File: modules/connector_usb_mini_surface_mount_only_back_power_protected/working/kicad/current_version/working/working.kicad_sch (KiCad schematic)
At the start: 2 parts, among them J1 scumnsmo

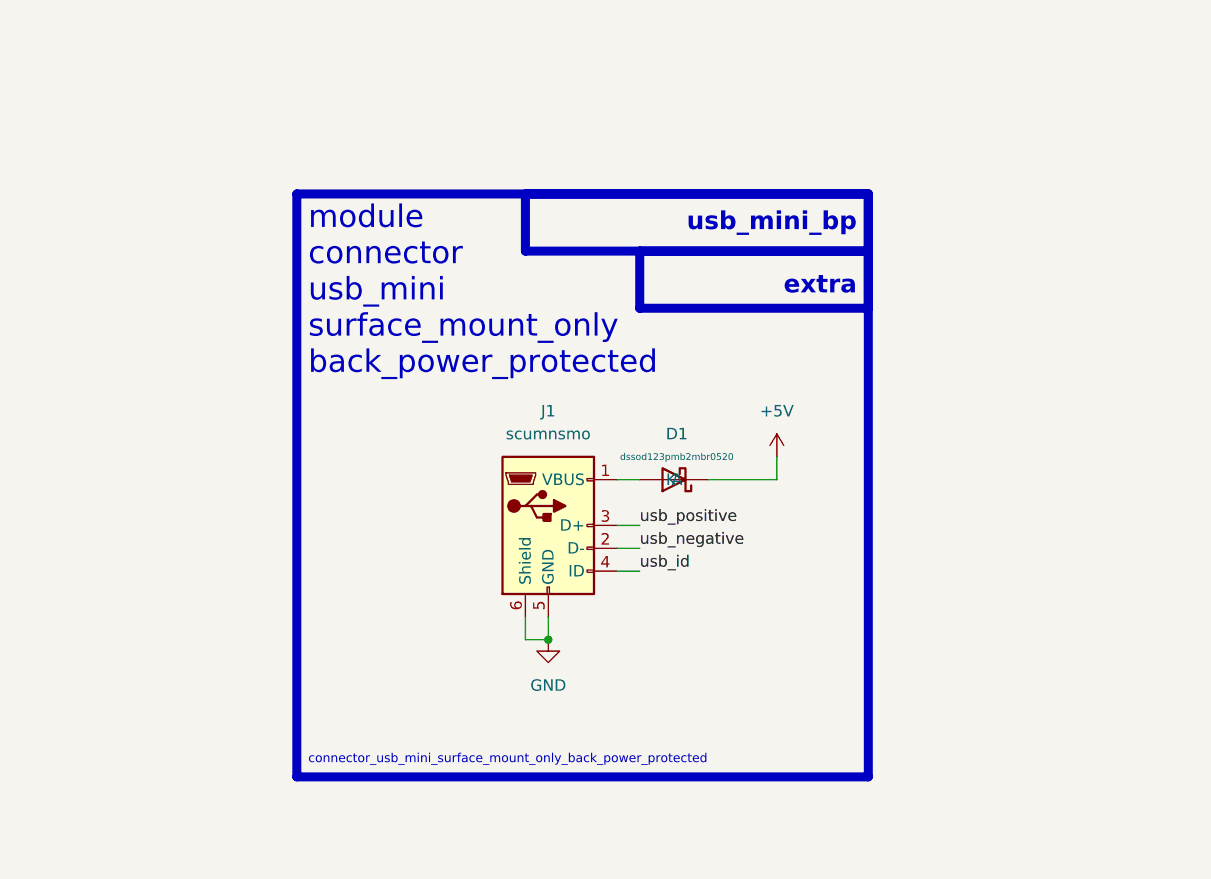
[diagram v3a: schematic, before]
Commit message: schematic formatting
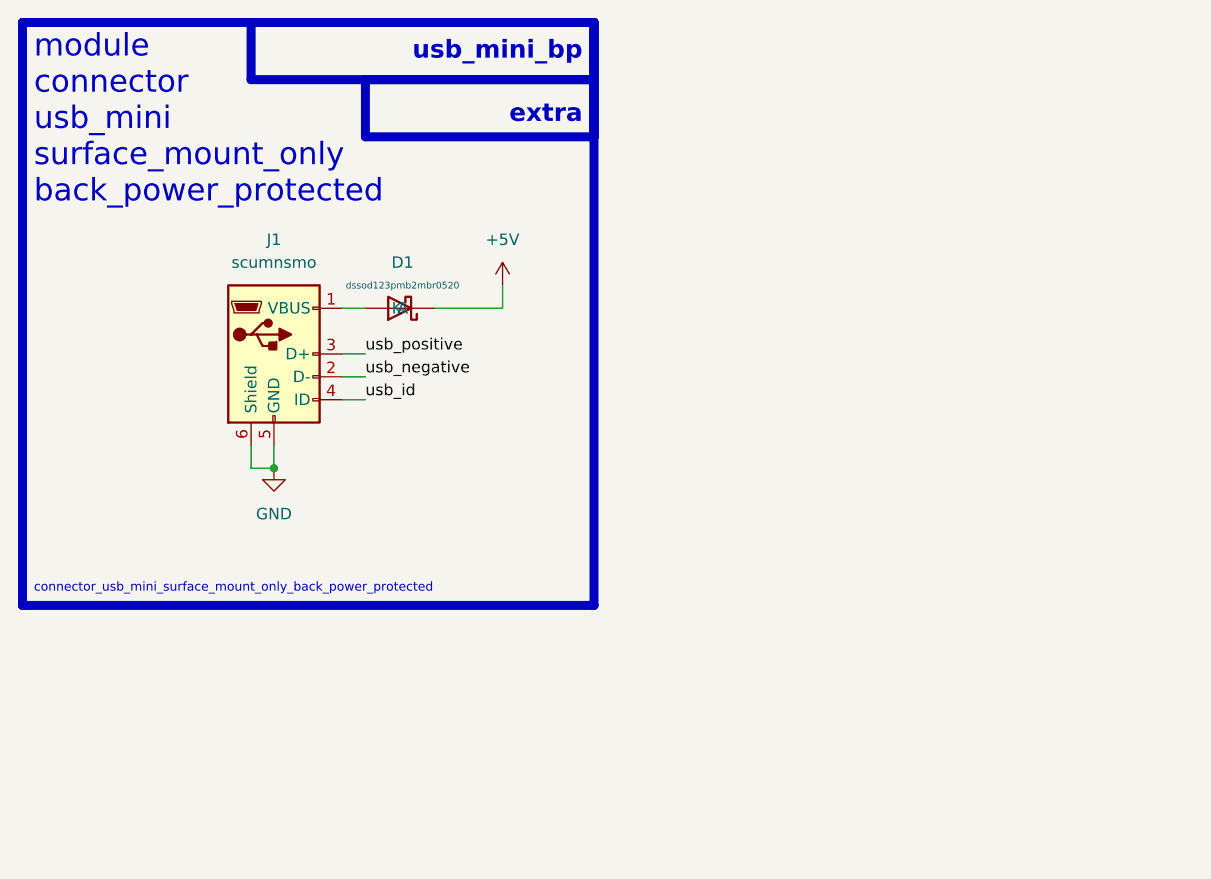
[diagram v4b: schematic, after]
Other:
- moved on the sheet: D1, J1
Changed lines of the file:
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@@
 (kicad_sch (version 20230121) (generator eeschema)
-  (paper "A4")
-  (junction (at 129.54 105.41) (diameter 0) (color 0 0 0 0)
+  (paper "A5")
+  (junction (at 99.06 86.36) (diameter 0) (color 0 0 0 0)
   )
-  (wire (pts (xy 129.54 102.87) (xy 129.54 105.41))
+  (wire (pts (xy 99.06 83.82) (xy 99.06 86.36))
     (stroke (width 0) (type default))
   )
-  (wire (pts (xy 137.16 87.63) (xy 139.7 87.63))
+  (wire (pts (xy 106.68 68.58) (xy 109.22 68.58))
     (stroke (width 0) (type default))
   )
-  (wire (pts (xy 137.16 97.79) (xy 139.7 97.79))
+  (wire (pts (xy 106.68 78.74) (xy 109.22 78.74))
     (stroke (width 0) (type default))
   )
-  (wire (pts (xy 137.16 95.25) (xy 139.7 95.25))
+  (wire (pts (xy 106.68 76.2) (xy 109.22 76.2))
     (stroke (width 0) (type default))
   )
-  (wire (pts (xy 154.94 85.09) (xy 154.94 87.63))
+  (wire (pts (xy 124.46 66.04) (xy 124.46 68.58))
     (stroke (width 0) (type default))
   )
-  (wire (pts (xy 154.94 87.63) (xy 147.32 87.63))
+  (wire (pts (xy 124.46 68.58) (xy 116.84 68.58))
     (stroke (width 0) (type default))
   )
-  (wire (pts (xy 127 105.41) (xy 129.54 105.41))
+  (wire (pts (xy 96.52 86.36) (xy 99.06 86.36))
     (stroke (width 0) (type default))
   )
-  (wire (pts (xy 127 102.87) (xy 127 105.41))
+  (wire (pts (xy 96.52 83.82) (xy 96.52 86.36))
     (stroke (width 0) (type default))
   )
-  (wire (pts (xy 137.16 92.71) (xy 139.7 92.71))
+  (wire (pts (xy 106.68 73.66) (xy 109.22 73.66))
     (stroke (width 0) (type default))
   )
-  (rectangle (start 127 55.88) (end 165.1 62.23)
+  (rectangle (start 96.52 36.83) (end 134.62 43.18)
     (stroke (width 1) (type default))
     (fill (type none))
   )
-  (rectangle (start 101.6 55.88) (end 165.1 120.65)
+  (rectangle (start 71.12 36.83) (end 134.62 101.6)
     (stroke (width 1) (type default))
     (fill (type none))
   )
-  (rectangle (start 139.7 62.23) (end 165.1 68.58)
+  (rectangle (start 109.22 43.18) (end 134.62 49.53)
     (stroke (width 1) (type default))
     (fill (type none))
   )
-  (text "usb_mini_bp\n\n" (at 163.83 63.5 0)
+  (text "usb_mini_bp\n\n" (at 133.35 44.45 0)
     (effects (font (size 2 2) (thickness 0.8) bold) (justify right bottom))
   )
   (text "connector_usb_mini_surface_mount_only_back_power_protected"
-    (at 102.87 119.38 0)
+    (at 72.39 100.33 0)
     (effects (font (size 1 1)) (justify left bottom))
   )
   (text "module\nconnector\nusb_mini\nsurface_mount_only\nback_power_protected\n"
-    (at 102.87 76.2 0)
+    (at 72.39 57.15 0)
     (effects (font (size 2.5 2.5)) (justify left bottom))
   )
-  (text "extra" (at 163.83 67.31 0)
+  (text "extra" (at 133.35 48.26 0)
     (effects (font (size 2 2) (thickness 0.8) bold) (justify right bottom))
   )
-  (label "usb_positive" (at 139.7 92.71 0) (fields_autoplaced)
+  (label "usb_positive" (at 109.22 73.66 0) (fields_autoplaced)
     (effects (font (size 1.27 1.27)) (justify left bottom))
   )
-  (label "usb_negative" (at 139.7 95.25 0) (fields_autoplaced)
+  (label "usb_negative" (at 109.22 76.2 0) (fields_autoplaced)
     (effects (font (size 1.27 1.27)) (justify left bottom))
   )
-  (label "usb_id" (at 139.7 97.79 0) (fields_autoplaced)
+  (label "usb_id" (at 109.22 78.74 0) (fields_autoplaced)
     (effects (font (size 1.27 1.27)) (justify left bottom))
   )
-  (symbol (lib_id "oomlout_oomp_part_symbols:dssod123pmb2mbr0520_electronic_diode_schottky_sod_123_package_marking_b2_mbr0520") (at 143.51 87.63 180) (unit 1)
+  (symbol (lib_id "oomlout_oomp_part_symbols:dssod123pmb2mbr0520_electronic_diode_schottky_sod_123_package_marking_b2_mbr0520") (at 113.03 68.58 180) (unit 1)
     (in_bom yes) (on_board yes) (dnp no) (fields_autoplaced)
-    (property "Reference" "D1" (at 143.8275 82.55 0)
+    (property "Reference" "D1" (at 113.3475 63.5 0)
       (effects (font (size 1.27 1.27)))
     )
-    (property "Value" "dssod123pmb2mbr0520" (at 143.8275 85.09 0)
+    (property "Value" "dssod123pmb2mbr0520" (at 113.3475 66.04 0)
       (effects (font (size 0.75 0.75)))
     )
-    (property "Footprint" "oomlout_oomp_part_footprints:dssod123pmb2mbr0520_electronic_diode_schottky_sod_123_package_marking_b2_mbr0520" (at 143.51 87.63 0)
+    (property "Footprint" "oomlout_oomp_part_footprints:dssod123pmb2mbr0520_electronic_diode_schottky_sod_123_package_marking_b2_mbr0520" (at 113.03 68.58 0)
       (effects (font (size 1.27 1.27)) hide)
     )
-    (property "Datasheet" "https://github.com/oomlout/oomlout_oomp_v3/parts/electronic_diode_schottky_sod_123_package_marking_b2_mbr0520/datasheet.pdf" (at 143.51 87.63 0)
+    (property "Datasheet" "https://github.com/oomlout/oomlout_oomp_v3/parts/electronic_diode_schottky_sod_123_package_marking_b2_mbr0520/datasheet.pdf" (at 113.03 68.58 0)
       (effects (font (size 1.27 1.27)) hide)
     )
@@
     )
   )
-  (symbol (lib_id "power:+5V") (at 154.94 85.09 0) (unit 1)
+  (symbol (lib_id "power:+5V") (at 124.46 66.04 0) (unit 1)
     (in_bom yes) (on_board yes) (dnp no) (fields_autoplaced)
-    (property "Reference" "#PWR013" (at 154.94 88.9 0)
+    (property "Reference" "#PWR013" (at 124.46 69.85 0)
       (effects (font (size 1.27 1.27)) hide)
     )
-    (property "Value" "+5V" (at 154.94 80.01 0)
+    (property "Value" "+5V" (at 124.46 60.96 0)
       (effects (font (size 1.27 1.27)))
     )
-    (property "Footprint" "" (at 154.94 85.09 0)
+    (property "Footprint" "" (at 124.46 66.04 0)
       (effects (font (size 1.27 1.27)) hide)
     )
-    (property "Datasheet" "" (at 154.94 85.09 0)
+    (property "Datasheet" "" (at 124.46 66.04 0)
       (effects (font (size 1.27 1.27)) hide)
     )
@@
     )
   )
-  (symbol (lib_id "oomlout_oomp_part_symbols:scumnsmo_electronic_socket_usb_mini_surface_mount_only") (at 129.54 92.71 0) (unit 1)
+  (symbol (lib_id "oomlout_oomp_part_symbols:scumnsmo_electronic_socket_usb_mini_surface_mount_only") (at 99.06 73.66 0) (unit 1)
     (in_bom yes) (on_board yes) (dnp no) (fields_autoplaced)
-    (property "Reference" "J1" (at 129.54 80.01 0)
+    (property "Reference" "J1" (at 99.06 60.96 0)
       (effects (font (size 1.27 1.27)))
     )
-    (property "Value" "scumnsmo" (at 129.54 82.55 0)
+    (property "Value" "scumnsmo" (at 99.06 63.5 0)
       (effects (font (size 1.27 1.27)))
     )
-    (property "Footprint" "oomlout_oomp_part_footprints:scumnsmo_electronic_socket_usb_mini_surface_mount_only" (at 133.35 93.98 0)
+    (property "Footprint" "oomlout_oomp_part_footprints:scumnsmo_electronic_socket_usb_mini_surface_mount_only" (at 102.87 74.93 0)
       (effects (font (size 1.27 1.27)) hide)
     )
-    (property "Datasheet" "https://github.com/oomlout/oomlout_oomp_v3/parts/electronic_socket_usb_mini_surface_mount_only/datasheet.pdf" (at 133.35 93.98 0)
+    (property "Datasheet" "https://github.com/oomlout/oomlout_oomp_v3/parts/electronic_socket_usb_mini_surface_mount_only/datasheet.pdf" (at 102.87 74.93 0)
       (effects (font (size 1.27 1.27)) hide)
     )
@@
     )
   )
-  (symbol (lib_id "power:GND") (at 129.54 105.41 0) (unit 1)
+  (symbol (lib_id "power:GND") (at 99.06 86.36 0) (unit 1)
     (in_bom yes) (on_board yes) (dnp no) (fields_autoplaced)
-    (property "Reference" "#PWR012" (at 129.54 111.76 0)
+    (property "Reference" "#PWR012" (at 99.06 92.71 0)
       (effects (font (size 1.27 1.27)) hide)
     )
-    (property "Value" "GND" (at 129.54 110.49 0)
+    (property "Value" "GND" (at 99.06 91.44 0)
       (effects (font (size 1.27 1.27)))
     )
-    (property "Footprint" "" (at 129.54 105.41 0)
+    (property "Footprint" "" (at 99.06 86.36 0)
       (effects (font (size 1.27 1.27)) hide)
     )
-    (property "Datasheet" "" (at 129.54 105.41 0)
+    (property "Datasheet" "" (at 99.06 86.36 0)
       (effects (font (size 1.27 1.27)) hide)
     )
